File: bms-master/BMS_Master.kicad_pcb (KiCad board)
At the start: 2 copper layers, 65 x 45 mm, 94 parts, among them J1 Conn_PWR, J2 Conn_CAN, J3 Conn_CSR, J4 PROG, J5 Conn_CSROUT, J6 BMS_M_IN, Q1 BC807, SW1 SW_SPST, U1 AP2204K-ADJ, U2 AP2204K-ADJ, U3 SN65HVD256D, U4 STM32F103C8Tx, U5 TLV2371DBV, U6 TLV2371DBV, U7 BQ79600-Q1, Y1 8M, Y2 32.768k

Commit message: chore: improve routing
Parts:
- moved C17 1.62 mm to (120.6, 51.9), turned to 90 degrees
- moved C16 1.30 mm to (113.1, 55.2)
- moved C1 0.84 mm to (81.4, 78.7)
- moved C2 0.50 mm to (76.4, 78.7)
- moved kibuzzard-679F55A0 0.30 mm to (89.9, 44.0)
- moved kibuzzard-67C3D8F9 0.20 mm to (93.6, 43.8)
- moved kibuzzard-67C3D9C1 0.20 mm to (109.2, 44.9)
- moved kibuzzard-679F55DD 0.10 mm to (77.5, 44.0)
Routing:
- net GND: track 37.4 -> 32.6 mm, vias 115 -> 106
- net SPI_RDY: track 18.2 -> 15.0 mm
- net VIO: track 162.7 -> 163.4 mm

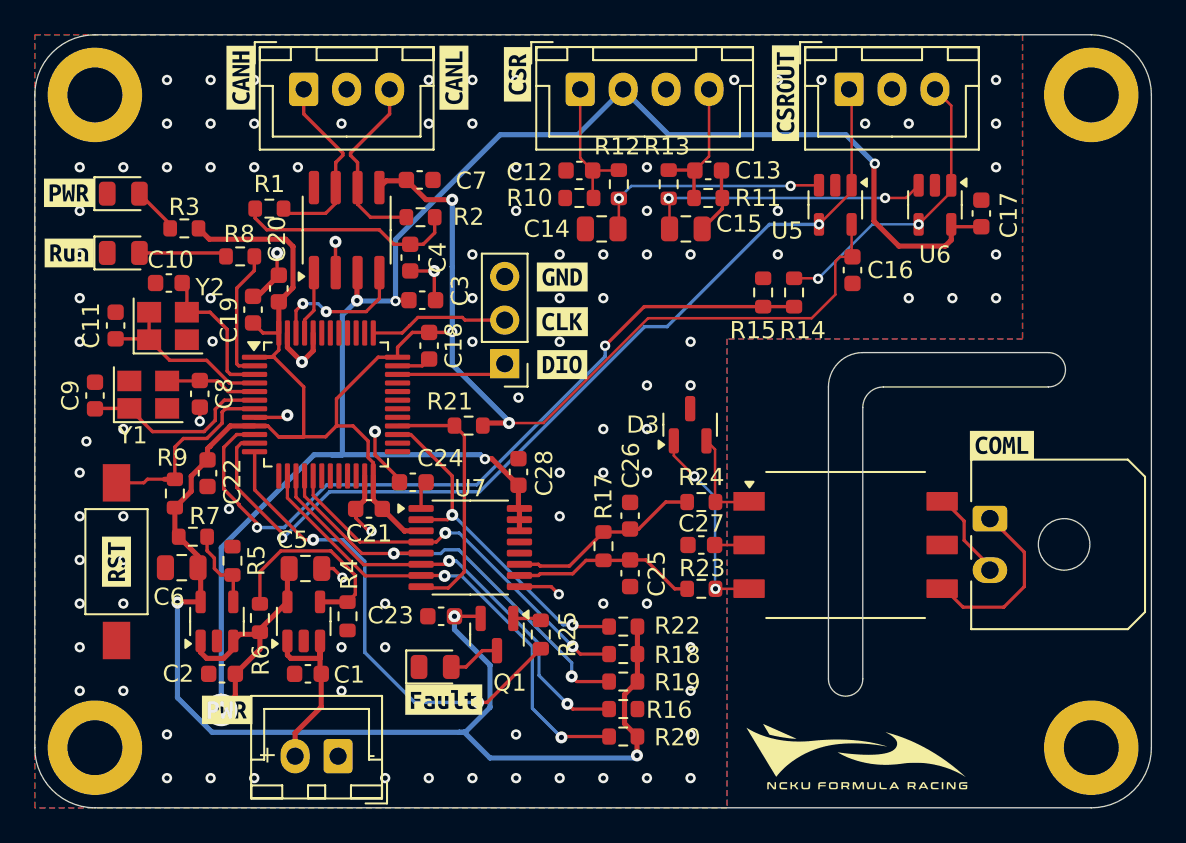
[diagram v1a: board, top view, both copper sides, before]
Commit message: fix: add bms fault connector
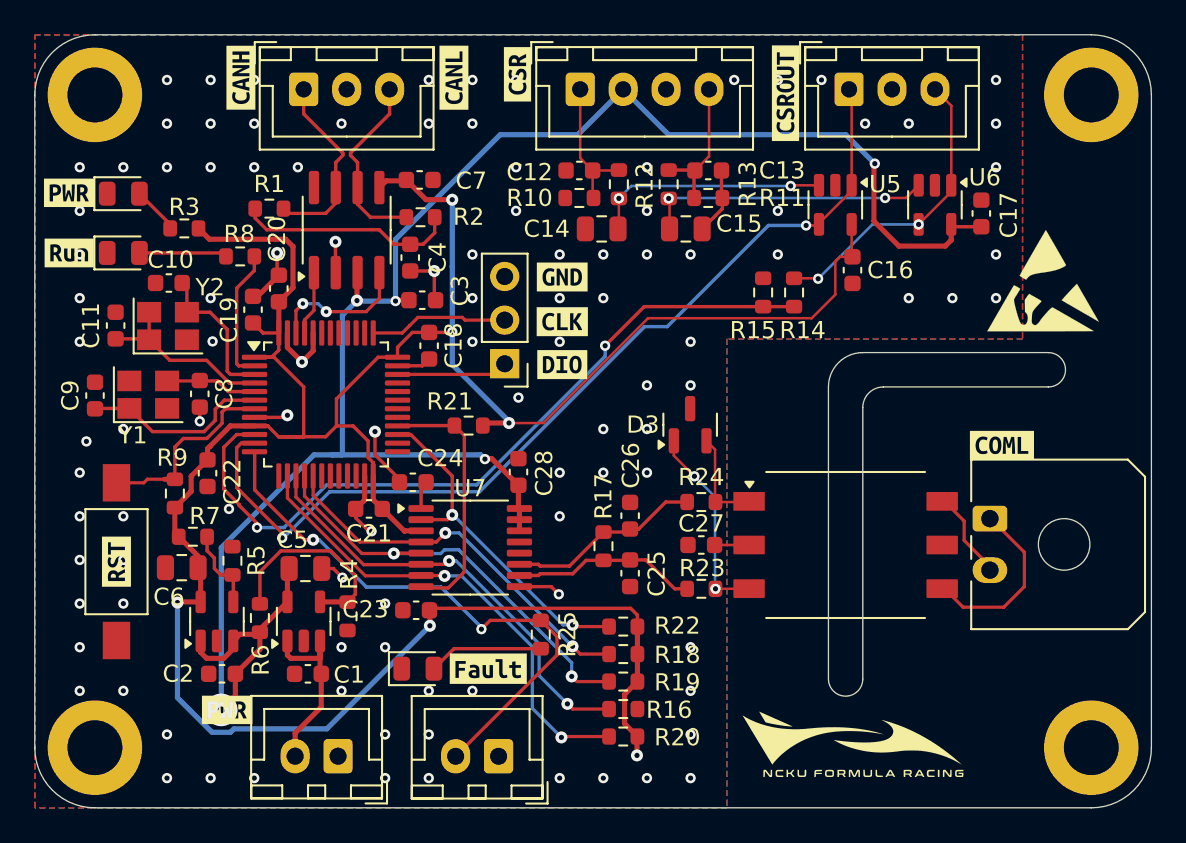
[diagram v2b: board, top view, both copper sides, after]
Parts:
- removed Q1: BC807, Package_TO_SOT_SMD:SOT-23
- added J7: Conn_Fault, Connector_JST:JST_XH_B2B-XH-A_1x02_P2.50mm_Vertical, F.Cu at (92.5, 83.5)
- added REF**: ESD-Logo_6.6x6mm_SilkScreen, Symbol:ESD-Logo_6.6x6mm_SilkScreen, F.Cu at (124.2, 55.8)
- R25: value 10K -> 10k
- moved kibuzzard-679F55F7 3.16 mm to (91.9, 78.4)
- moved C23 1.50 mm to (87.7, 75.0)
- moved D4 1.01 mm to (87.8, 78.4)
- moved G*** 0.75 mm to (113.2, 82.8)
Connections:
- R25 pad 1: Net-(Q1-B) -> BMS_FAULT
- R25 pad 2: BMS_FAULT -> Net-(D4-A)
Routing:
- net VIO: track 163.4 -> 157.0 mm
- net BMS_FAULT: track 28.4 -> 33.3 mm
- net Net-(D4-A): track 3.06 -> 6.70 mm
- net Net-(Q1-B): track 1.65 -> 0.00 mm
- net GND: vias 106 -> 104
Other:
- board text removed: "+ -"

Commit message: feat: improve diff signal
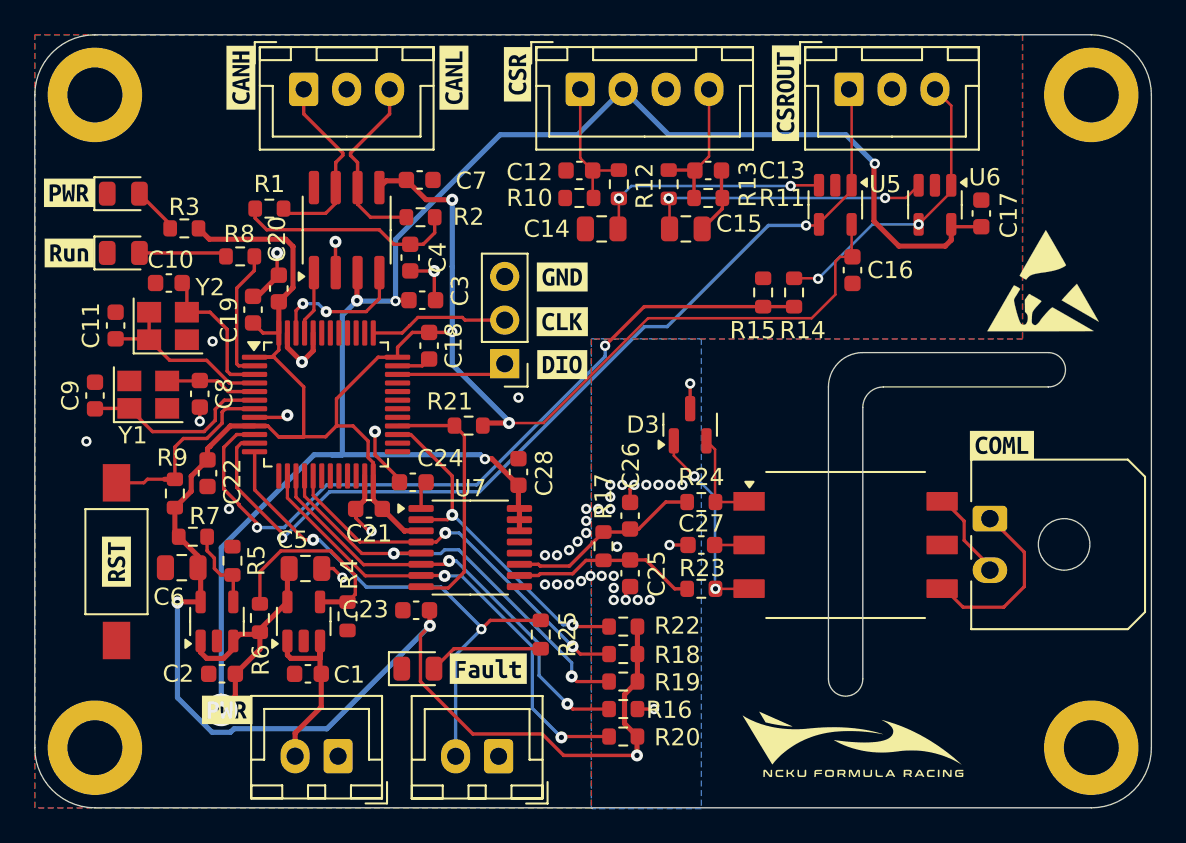
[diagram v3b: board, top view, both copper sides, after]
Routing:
- net VIO: track 157.0 -> 161.9 mm
- net GND: track 32.6 -> 35.7 mm, vias 104 -> 44
- net BMS_FAULT: track 33.3 -> 30.5 mm

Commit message: Redo BMS master layout again, SD card slot added
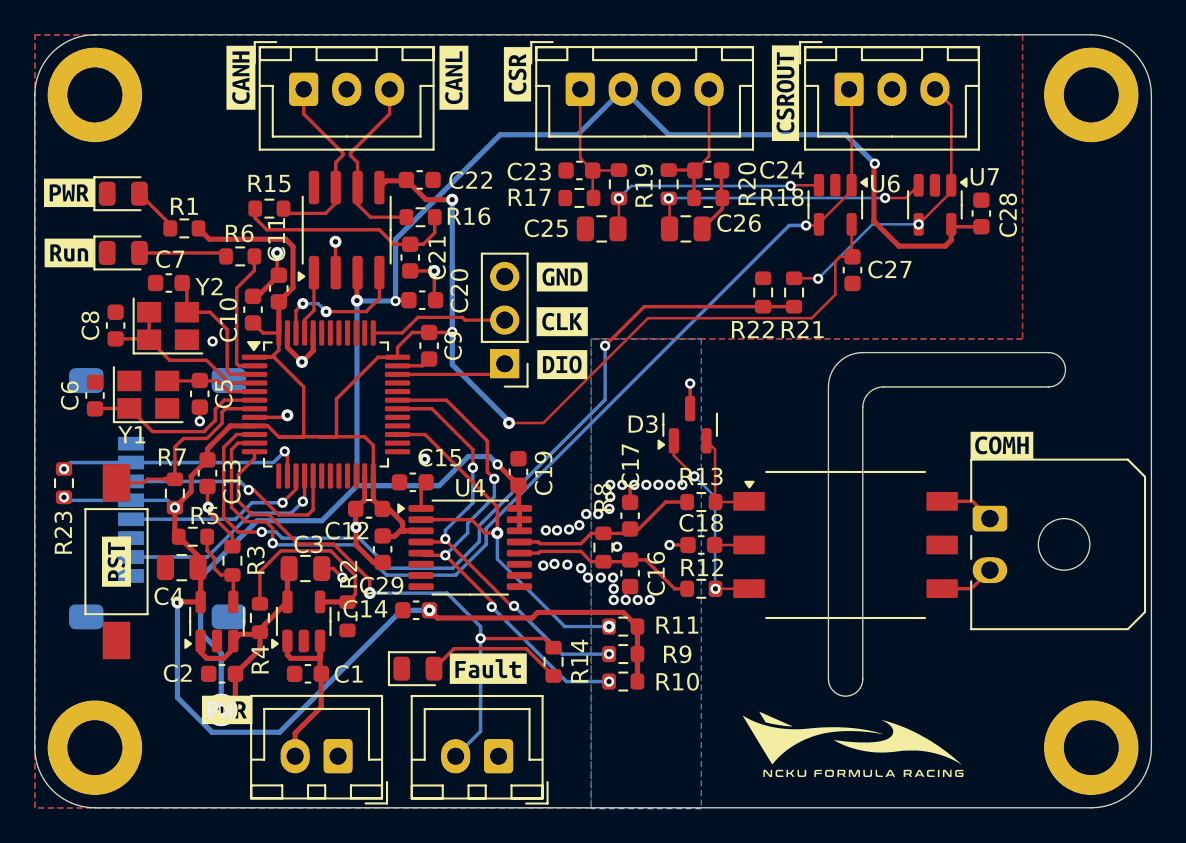
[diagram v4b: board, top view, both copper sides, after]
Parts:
- removed the R16 at (99.8, 80.8)
- removed the R20 at (99.8, 82.3)
- removed the R21 at (90.8, 64.2)
- removed REF**: ESD-Logo_6.6x6mm_SilkScreen, Symbol:ESD-Logo_6.6x6mm_SilkScreen
- removed kibuzzard-679F551A: G***, kibuzzard-679F551A
- removed kibuzzard-67C3D81C: G***, kibuzzard-67C3D81C
- added C29: 100n, Capacitor_SMD:C_0603_1608Metric, F.Cu at (85.8, 71.5)
- added J8: Micro_SD_Card, Connector_Card:microSD_HC_Molex_47219-2001, B.Cu at (73.2, 68.5)
- added R23: 1K, Resistor_SMD:R_0603_1608Metric, F.Cu at (67.2, 67.6)
- added kibuzzard-67D6AC10: G***, kibuzzard-67D6AC10, F.Cu at (121.8, 65.4)
- added kibuzzard-67D6BCA3: G***, kibuzzard-67D6BCA3, B.Cu at (113.5, 84.4)
- moved R14 1.75 mm to (95.7, 78.0)
- moved R8 0.08 mm to (98.6, 71.3)
- renumbered C19 to C10, C20 to C11, C21 to C12, C22 to C13, C23 to C14, C24 to C15, C25 to C16, C26 to C17, C27 to C18, C28 to C19, C3 to C20, C4 to C21, C7 to C22, C12 to C23, C13 to C24, C14 to C25, C15 to C26, C16 to C27, C17 to C28, C5 to C3, C6 to C4, C8 to C5, C9 to C6, C10 to C7, C11 to C8, C18 to C9, J4 to J2, J7 to J3, J6 to J4, J2 to J5, J3 to J6, J5 to J7, R3 to R1, R19 to R10, R22 to R11, R23 to R12, R24 to R13, R25 to R14, R1 to R15, R2 to R16, R10 to R17, R11 to R18, R12 to R19, R4 to R2, R13 to R20, R14 to R21, R15 to R22, R5 to R3, R6 to R4, R7 to R5, R8 to R6, R9 to R7, R17 to R8, R18 to R9, U4 to U3, U7 to U4, U3 to U5, U5 to U6, U6 to U7
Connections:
- C16 pad 1: COMLP -> COMHN
- C17 pad 1: COMLN -> COMHP
- J4 pad 1: Net-(J6-Pin_1) (its old number) -> Net-(J4-Pin_1)
- J4 pad 2: Net-(J6-Pin_2) -> Net-(J4-Pin_2)
- R10 pad 2: MISO -> UART_RX
- R12 pad 1: COMLP -> COMHN
- R13 pad 1: COMLN -> COMHP
- R8 pad 1: COMLP -> COMHN
- R8 pad 2: COMLN -> COMHP
- R9 pad 2: MOSI -> UART_TX
- TR1 pad 4: Net-(J6-Pin_1) (its old number) -> Net-(J4-Pin_2)
- TR1 pad 6: Net-(J6-Pin_2) -> Net-(J4-Pin_1)
- U3 pad 14: nCS -> CS
- U3 pad 28: SPI_RDY -> unconnected-(U3-PB15-Pad28)
- U3 pad 30: unconnected-(U4-PA9-Pad30) -> UART_TX
- U3 pad 31: unconnected-(U4-PA10-Pad31) -> UART_RX
- U4 pad 10: COMLP -> unconnected-(U4-COMLP-Pad10)
- U4 pad 11: COMLN -> unconnected-(U4-COMLN-Pad11)
- U4 pad 12: unconnected-(U7-COMHN-Pad12) -> COMHN
- U4 pad 13: unconnected-(U7-COMHP-Pad13) -> COMHP
- U4 pad 4: MOSI -> UART_TX
- U4 pad 5: MISO -> UART_RX
- U4 pad 6: SCLK -> GND
- U4 pad 7: nCS -> GND
- U4 pad 8: SPI_RDY -> GND
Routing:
- net UART_RX: track 0.00 -> 28.4 mm, vias 0 -> 4
- net nCS: track 27.9 -> 0.00 mm, vias 2 -> 0
- net UART_TX: track 0.00 -> 25.1 mm, vias 0 -> 4
- net SPI_RDY: track 15.0 -> 0.00 mm
- net CS: track 0.00 -> 14.8 mm, vias 0 -> 2
- net SCLK: track 25.8 -> 11.1 mm, vias 2 -> 1
- net MISO: track 25.6 -> 12.9 mm, vias 2 -> 1
- net COMLN: track 11.3 -> 0.00 mm
- net Net-(J6-Pin_1) (its old number): track 10.8 -> 0.00 mm
- net COMLP: track 10.8 -> 0.00 mm
- net COMHP: track 0.00 -> 10.8 mm
- net COMHN: track 0.00 -> 10.8 mm
- net MOSI: track 22.6 -> 13.5 mm, vias 2 -> 1
- net Net-(J6-Pin_2): track 5.14 -> 0.00 mm
- net CRS1_DIV: track 44.5 -> 49.3 mm
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
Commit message: Further update layout detail to improve clearance
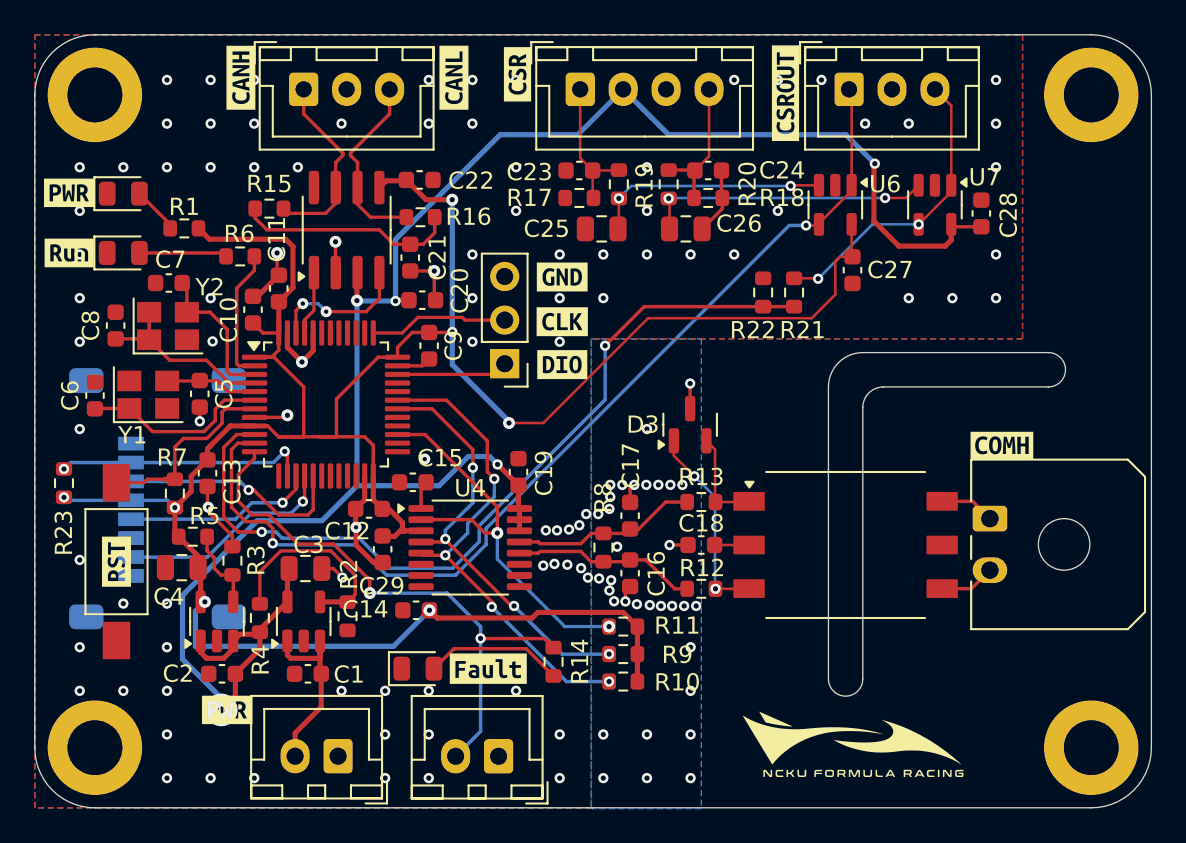
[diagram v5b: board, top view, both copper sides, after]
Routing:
- net VIO: track 159.4 -> 151.6 mm
- net +5V: track 111.9 -> 112.8 mm
- net GND: track 37.6 -> 37.7 mm, vias 41 -> 128

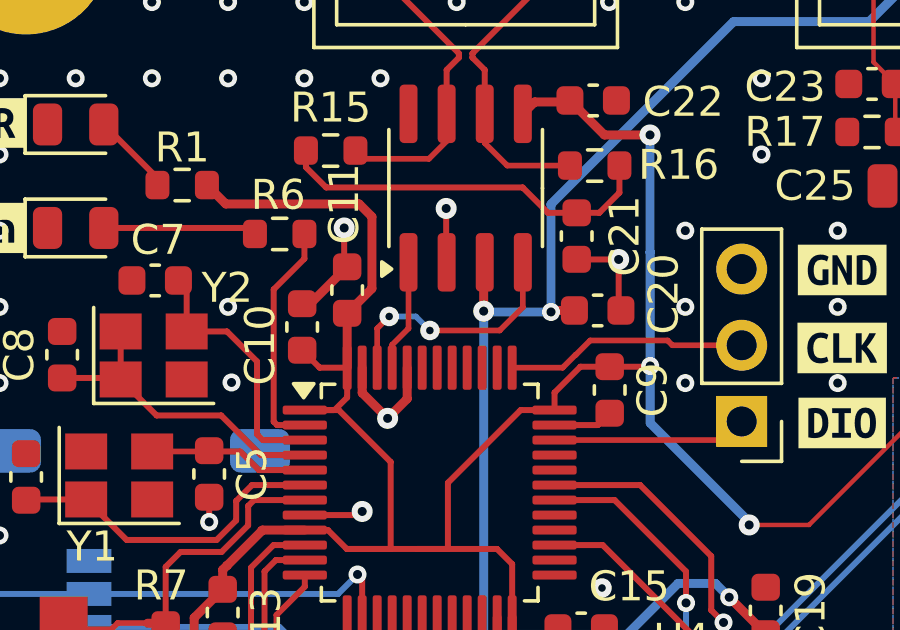
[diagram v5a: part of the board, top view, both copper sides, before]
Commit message: Fix bms master can bus tx/rx opposite issue
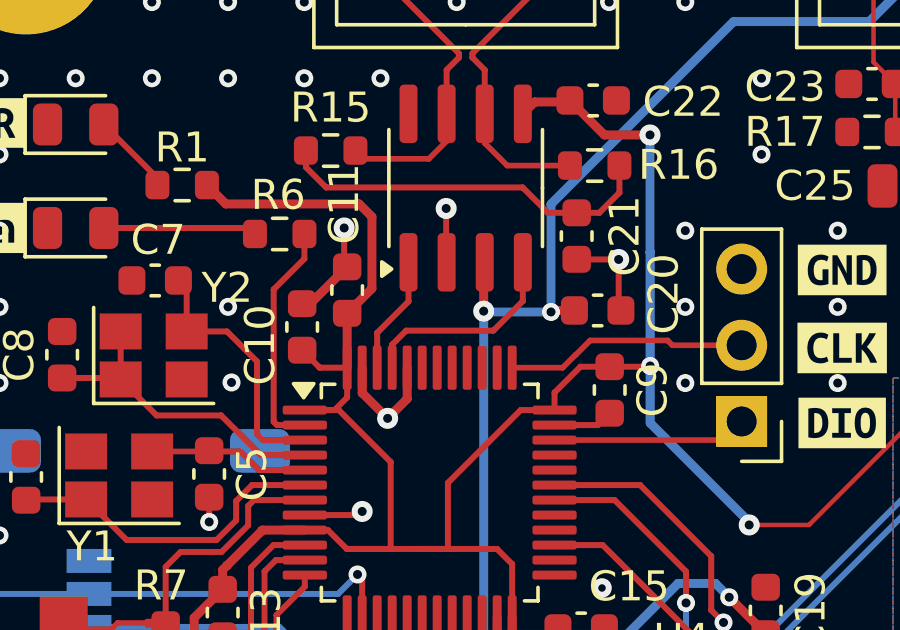
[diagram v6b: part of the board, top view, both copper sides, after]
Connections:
- U5 pad 1: CAN_RX -> CAN_TX
- U5 pad 4: CAN_TX -> CAN_RX
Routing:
- net CAN_TX: track 8.34 -> 3.95 mm, vias 2 -> 0
- net CAN_RX: track 3.74 -> 7.02 mm
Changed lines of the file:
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@@
       (stroke (width 0.1) (type solid)) (layer "F.Fab"))
     (pad "1" smd roundrect (at -2.475 -1.905 90) (size 1.95 0.6) (layers "F.Cu" "F.Paste" "F.Mask") (roundrect_rratio 0.25)
-      (net 56 "CAN_RX") (pinfunction "TXD") (pintype "input"))
+      (net 57 "CAN_TX") (pinfunction "TXD") (pintype "input"))
     (pad "2" smd roundrect (at -2.475 -0.635 90) (size 1.95 0.6) (layers "F.Cu" "F.Paste" "F.Mask") (roundrect_rratio 0.25)
       (net 1 "GND") (pinfunction "GND") (pintype "power_in"))
@@
       (net 3 "+5V") (pinfunction "VCC") (pintype "power_in"))
     (pad "4" smd roundrect (at -2.475 1.905 90) (size 1.95 0.6) (layers "F.Cu" "F.Paste" "F.Mask") (roundrect_rratio 0.25)
-      (net 57 "CAN_TX") (pinfunction "RXD") (pintype "output"))
+      (net 56 "CAN_RX") (pinfunction "RXD") (pintype "output"))
     (pad "5" smd roundrect (at 2.475 1.905 90) (size 1.95 0.6) (layers "F.Cu" "F.Paste" "F.Mask") (roundrect_rratio 0.25)
       (net 4 "VIO") (pinfunction "VRXD") (pintype "power_in"))
@@
   (segment (start 90.7 69.95) (end 90.7 70.5) (width 0.2) (layer "B.Cu") (net 47))
   (segment (start 90.7 70.5) (end 89.4 71.8) (width 0.2) (layer "B.Cu") (net 47))
-  (segment (start 81.205 58.094662) (end 81.75 57.549662) (width 0.19) (layer "F.Cu") (net 56))
-  (segment (start 81.75 57.549662) (end 81.75 55.345) (width 0.19) (layer "F.Cu") (net 56))
-  (segment (start 81.205 58.8575) (end 81.205 58.094662) (width 0.19) (layer "F.Cu") (net 56))
-  (segment (start 85.56 56.845) (end 85.56 55.345) (width 0.19) (layer "F.Cu") (net 57))
-  (segment (start 80.705 57.55) (end 80.705 58.8575) (width 0.19) (layer "F.Cu") (net 57))
-  (segment (start 81.105 57.15) (end 80.705 57.55) (width 0.19) (layer "F.Cu") (net 57))
-  (segment (start 82.46315 57.617701) (end 84.787299 57.617701) (width 0.19) (layer "F.Cu") (net 57))
-  (segment (start 84.787299 57.617701) (end 85.56 56.845) (width 0.19) (layer "F.Cu") (net 57))
-  (via (at 82.46315 57.617701) (size 0.65) (drill 0.25) (layers "F.Cu" "B.Cu") (net 57))
-  (via (at 81.105 57.15) (size 0.65) (drill 0.25) (layers "F.Cu" "B.Cu") (net 57))
-  (segment (start 82.46315 57.617701) (end 81.995449 57.15) (width 0.19) (layer "B.Cu") (net 57))
-  (segment (start 81.995449 57.15) (end 81.105 57.15) (width 0.19) (layer "B.Cu") (net 57))
+  (segment (start 81.669889 57.622701) (end 84.577299 57.622701) (width 0.2) (layer "F.Cu") (net 56))
+  (segment (start 84.577299 57.622701) (end 85.56 56.64) (width 0.2) (layer "F.Cu") (net 56))
+  (segment (start 81.205 58.8575) (end 81.205 58.08759) (width 0.2) (layer "F.Cu") (net 56))
+  (segment (start 81.205 58.08759) (end 81.669889 57.622701) (width 0.2) (layer "F.Cu") (net 56))
+  (segment (start 85.56 56.64) (end 85.56 55.345) (width 0.2) (layer "F.Cu") (net 56))
+  (segment (start 80.705 58.8575) (end 80.705 57.695) (width 0.2) (layer "F.Cu") (net 57))
+  (segment (start 81.75 56.65) (end 81.75 55.345) (width 0.2) (layer "F.Cu") (net 57))
+  (segment (start 80.705 57.695) (end 81.75 56.65) (width 0.2) (layer "F.Cu") (net 57))
   (zone (net 1) (net_name "GND") (layers "F&B.Cu") (hatch edge 0.5)
     (connect_pads (clearance 0.25))
